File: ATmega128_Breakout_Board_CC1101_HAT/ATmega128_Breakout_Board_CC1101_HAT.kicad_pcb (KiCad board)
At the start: 2 copper layers, 48.9 x 49.1 mm, 33 parts, among them J10 17-32, J11 49-64, J12 3V I2C, J7 LCD, J8 1-16, J9 33-48, Q1 BCX54, Q2 BCX54, Q3 BCX54, SW1 Config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

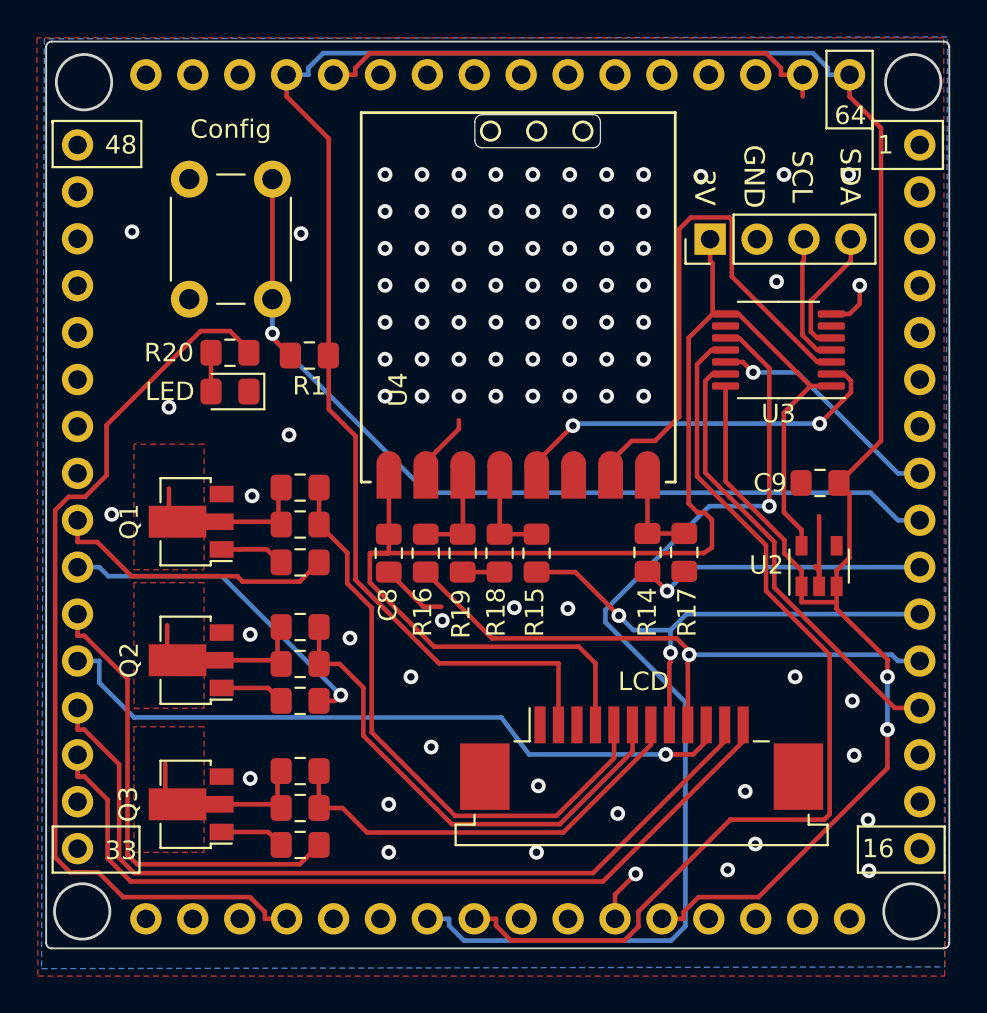
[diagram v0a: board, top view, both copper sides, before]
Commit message: board update for new kicad version
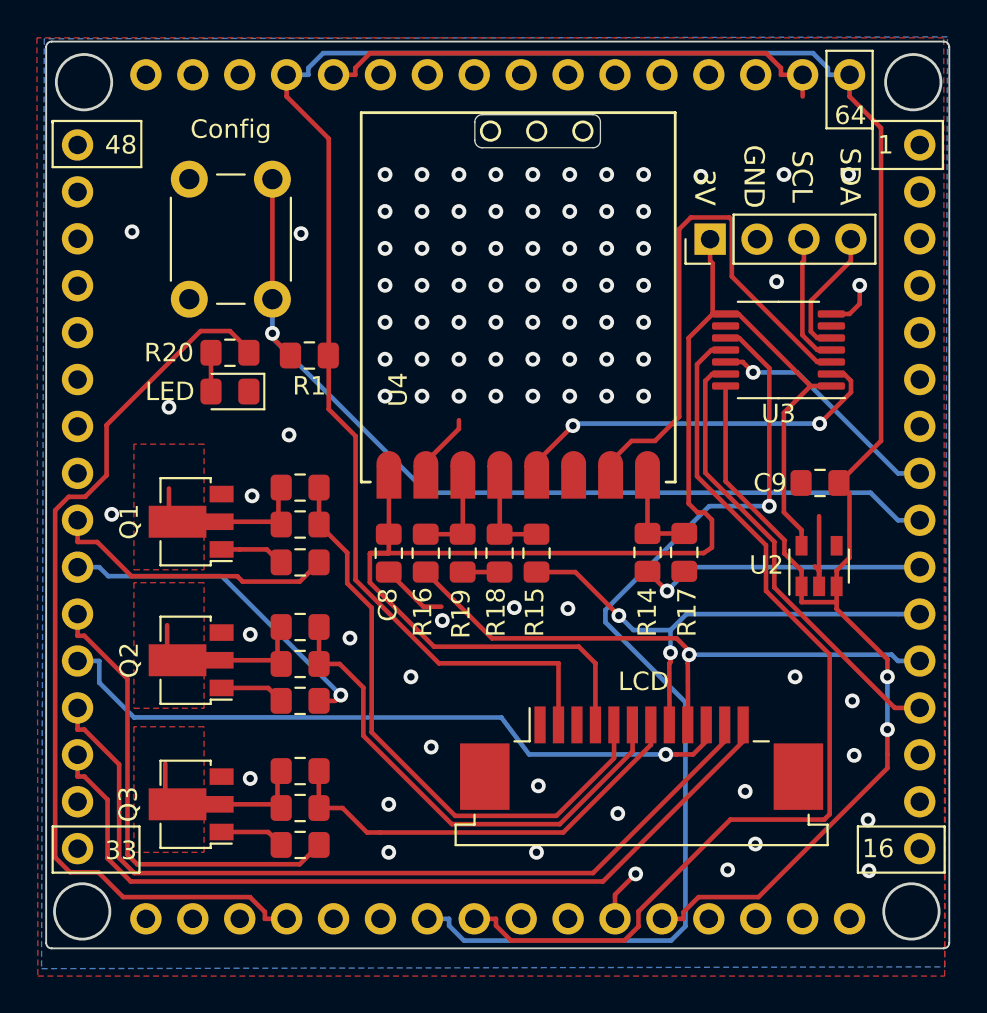
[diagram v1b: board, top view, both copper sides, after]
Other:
- net class Default removed
